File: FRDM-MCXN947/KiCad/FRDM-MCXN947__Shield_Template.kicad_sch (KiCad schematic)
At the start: 10 parts, among them J1 ${ALTIUM_VALUE}, J12 ${ALTIUM_VALUE}, J2 ${ALTIUM_VALUE}, J3 ${ALTIUM_VALUE}, J4 ${ALTIUM_VALUE}, J9 ${ALTIUM_VALUE}

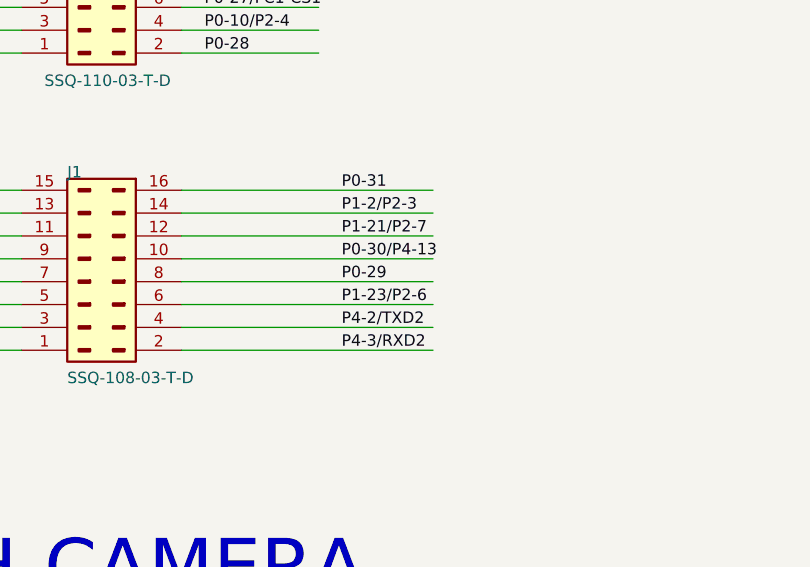
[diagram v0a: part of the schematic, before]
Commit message: fixed bug in N947 template on J1.  P0-29 and P1-23 were flopped
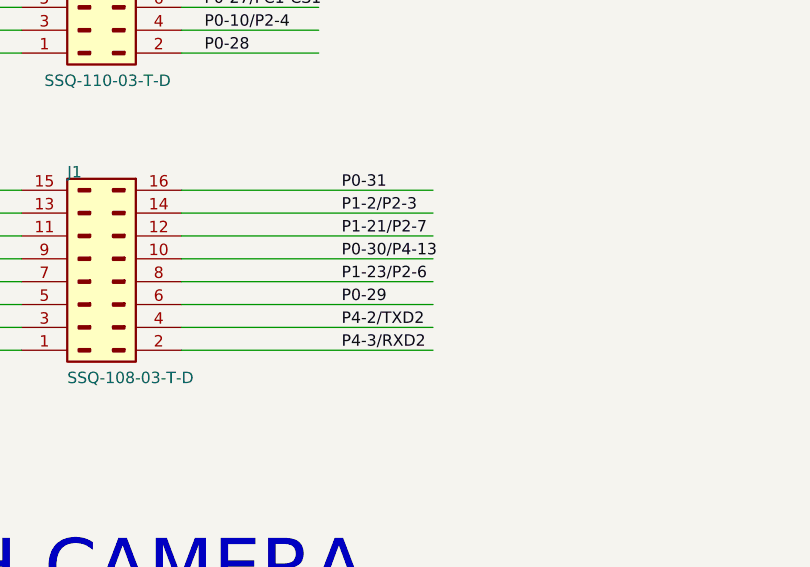
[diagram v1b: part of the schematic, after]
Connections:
- net P0-29: now also J1.6 (Pin_6); no longer J1.8 (Pin_8)
- net P1-23/P2-6: now also J1.8 (Pin_8); no longer J1.6 (Pin_6)
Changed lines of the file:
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@@
-    (effects (font (size 1.27 1.27)) (justify left bottom))
-  )
-  (label "P1-23/P2-6" (at 312.42 119.38 0) (fields_autoplaced)
     (effects (font (size 1.27 1.27)) (justify left bottom))
   )
   (label "P0-28" (at 297.18 91.44 0) (fields_autoplaced)
-    (effects (font (size 1.27 1.27)) (justify left bottom))
-  )
-  (label "P0-29" (at 312.42 116.84 0) (fields_autoplaced)
     (effects (font (size 1.27 1.27)) (justify left bottom))
   )
@@
     (effects (font (size 1.27 1.27)) (justify left bottom))
   )
+  (label "P0-29" (at 312.42 119.38 0) (fields_autoplaced)
+    (effects (font (size 1.27 1.27)) (justify left bottom))
+  )
   (label "P4-1/P1-17" (at 297.18 68.58 0) (fields_autoplaced)
     (effects (font (size 1.27 1.27)) (justify left bottom))
@@
     (effects (font (size 1.27 1.27)) (justify left bottom))
   )
+  (label "P1-23/P2-6" (at 312.42 116.84 0) (fields_autoplaced)
+    (effects (font (size 1.27 1.27)) (justify left bottom))
+  )
